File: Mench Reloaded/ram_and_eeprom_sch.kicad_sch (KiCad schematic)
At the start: 25 parts, among them J1 XBUS_265, J10 FTDI serial, J11 Power Sel, J2 TGx, J3 RAM CSB select, J4 P4x, J5 P5x, J6 P6x, J7 68c256 Sel, J8 DC Power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

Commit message: Changed EEPROM footprint to use low profile ZIF socket. Moved components and traces to make space for socket. Moved some resistors to the front side of the board.
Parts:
- U3: footprint Package_DIP:DIP-28_W15.24mm_Socket -> Socket:DIP-28_W15.24mm_LowProfileZifSocket
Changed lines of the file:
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@@
 			)
 		)
-		(property "Footprint" "Package_DIP:DIP-28_W15.24mm_Socket"
+		(property "Footprint" "Socket:DIP-28_W15.24mm_LowProfileZifSocket"
 			(at 175.26 48.26 0)
 			(effects

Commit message: Added power symbols and no connect to eliminate ERC errors.
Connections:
- no-connect marks 0 -> 1

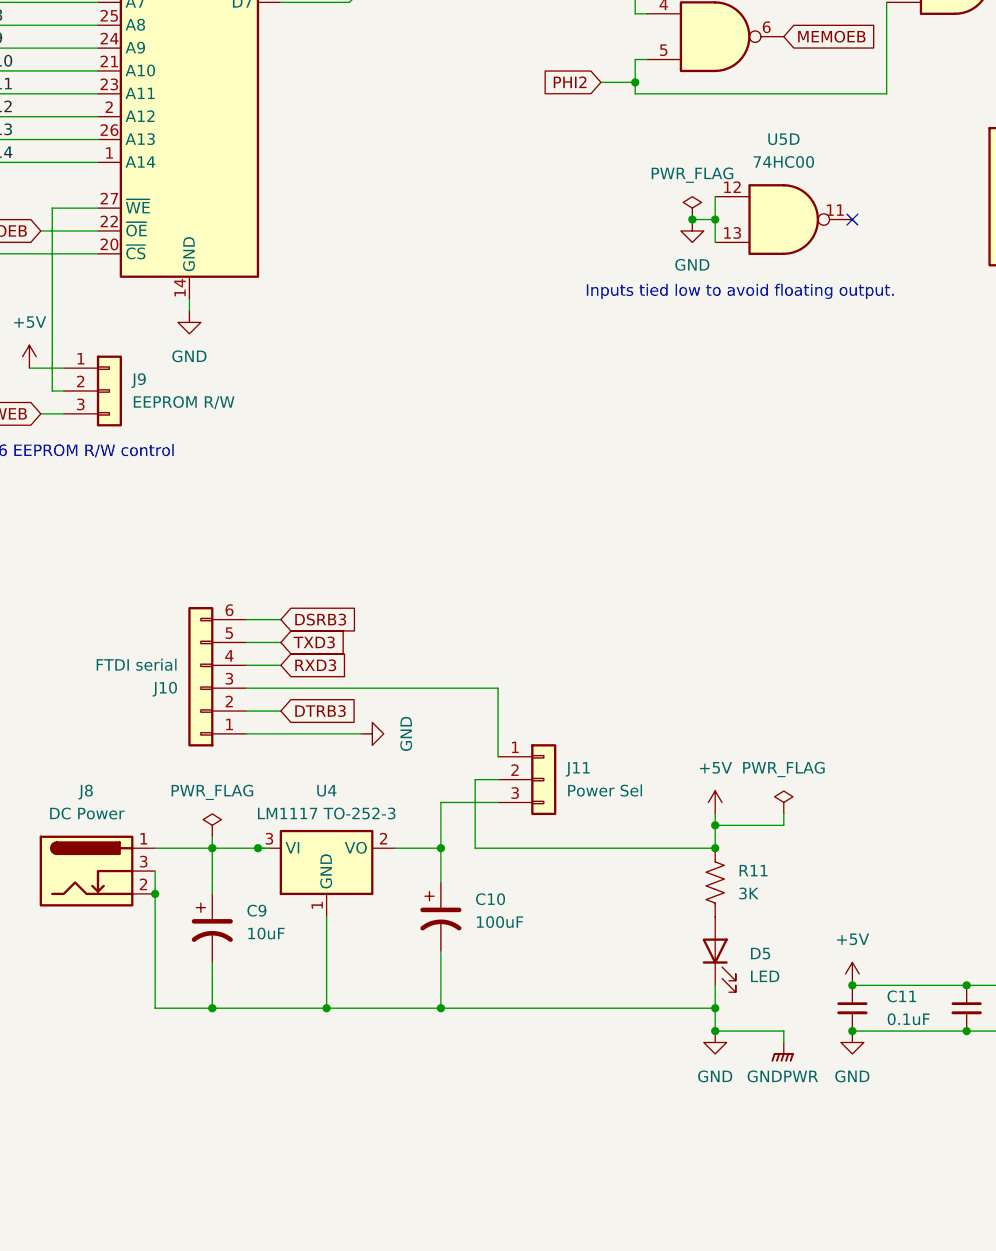
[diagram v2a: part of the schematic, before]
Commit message: Corrected all errors and most warnings after a ERC inspection.
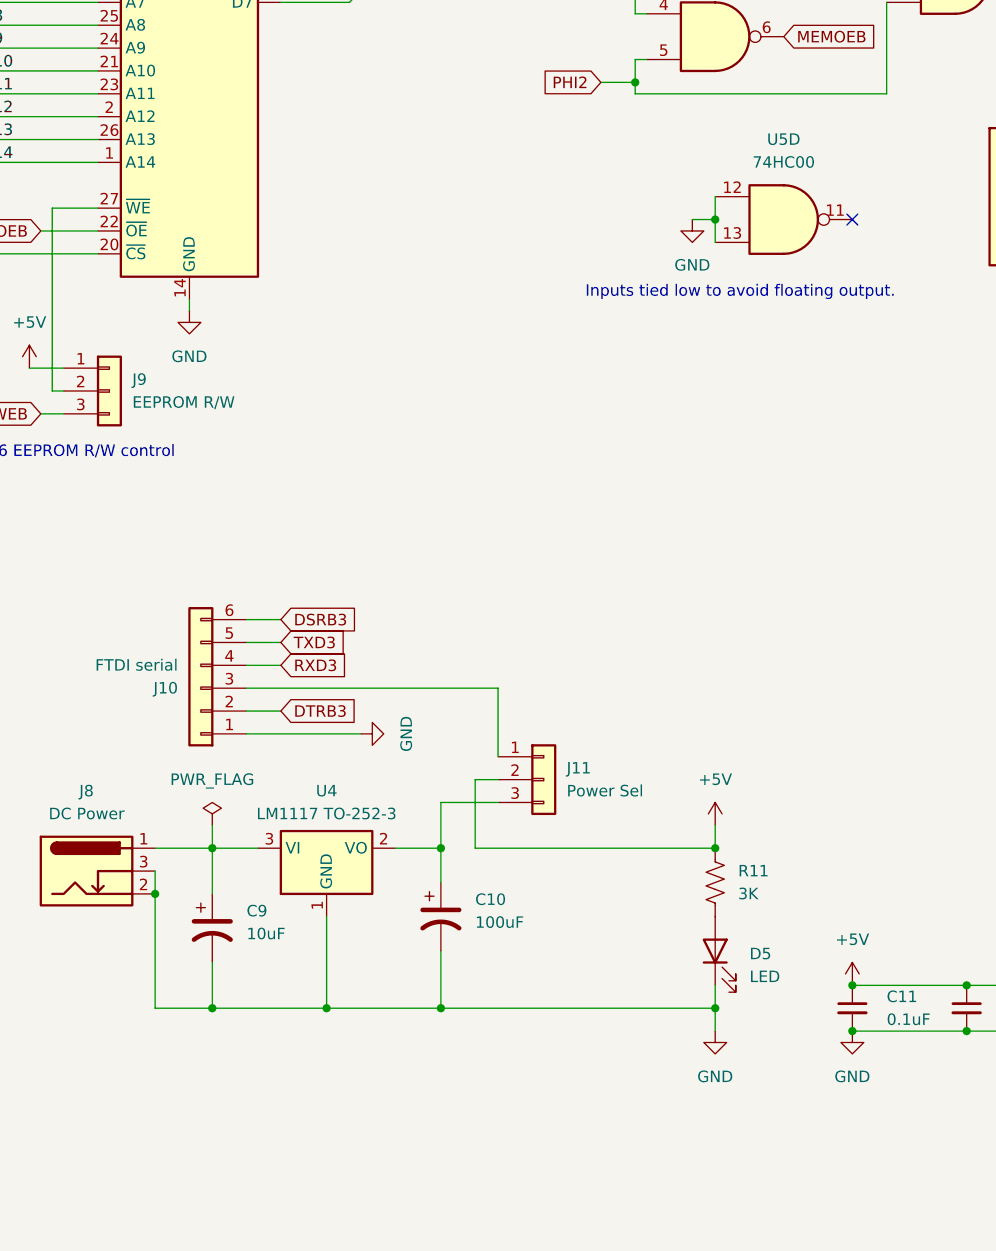
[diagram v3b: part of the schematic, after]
